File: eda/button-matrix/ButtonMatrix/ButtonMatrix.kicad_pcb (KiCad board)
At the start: 2 copper layers, 87.2 x 87.2 mm, 53 parts, among them SW1 SW_Omron_B3FS, SW10 SW_Omron_B3FS, SW11 SW_Omron_B3FS, SW12 SW_Omron_B3FS, SW13 SW_Omron_B3FS, SW14 SW_Omron_B3FS, SW15 SW_Omron_B3FS, SW16 SW_Omron_B3FS, SW2 SW_Omron_B3FS, SW3 SW_Omron_B3FS, SW4 SW_Omron_B3FS, SW5 SW_Omron_B3FS, SW6 SW_Omron_B3FS, SW7 SW_Omron_B3FS, SW8 SW_Omron_B3FS, SW9 SW_Omron_B3FS

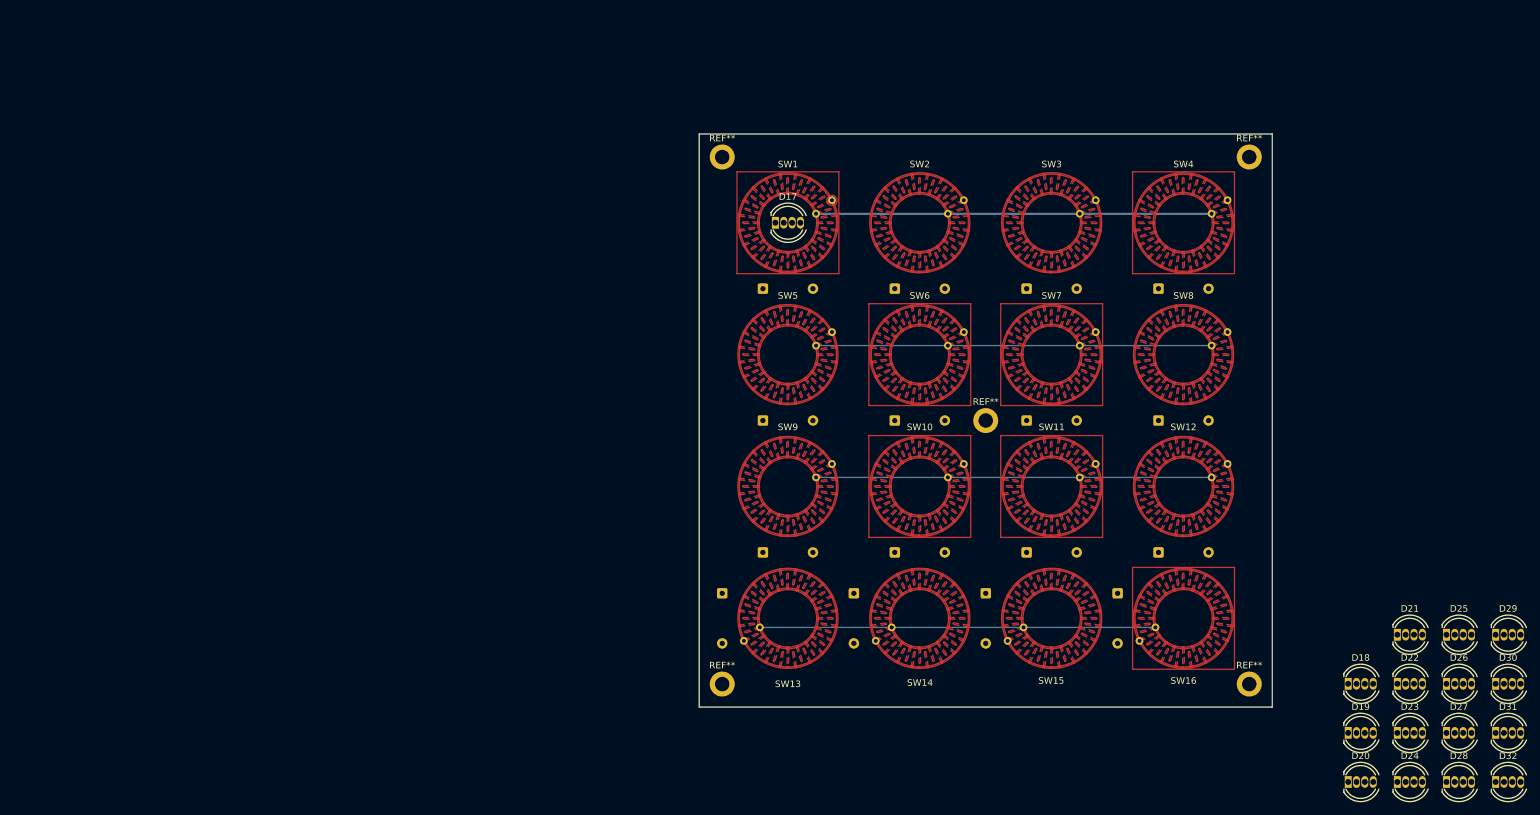
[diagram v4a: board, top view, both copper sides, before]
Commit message: - Added headers and connected all diods
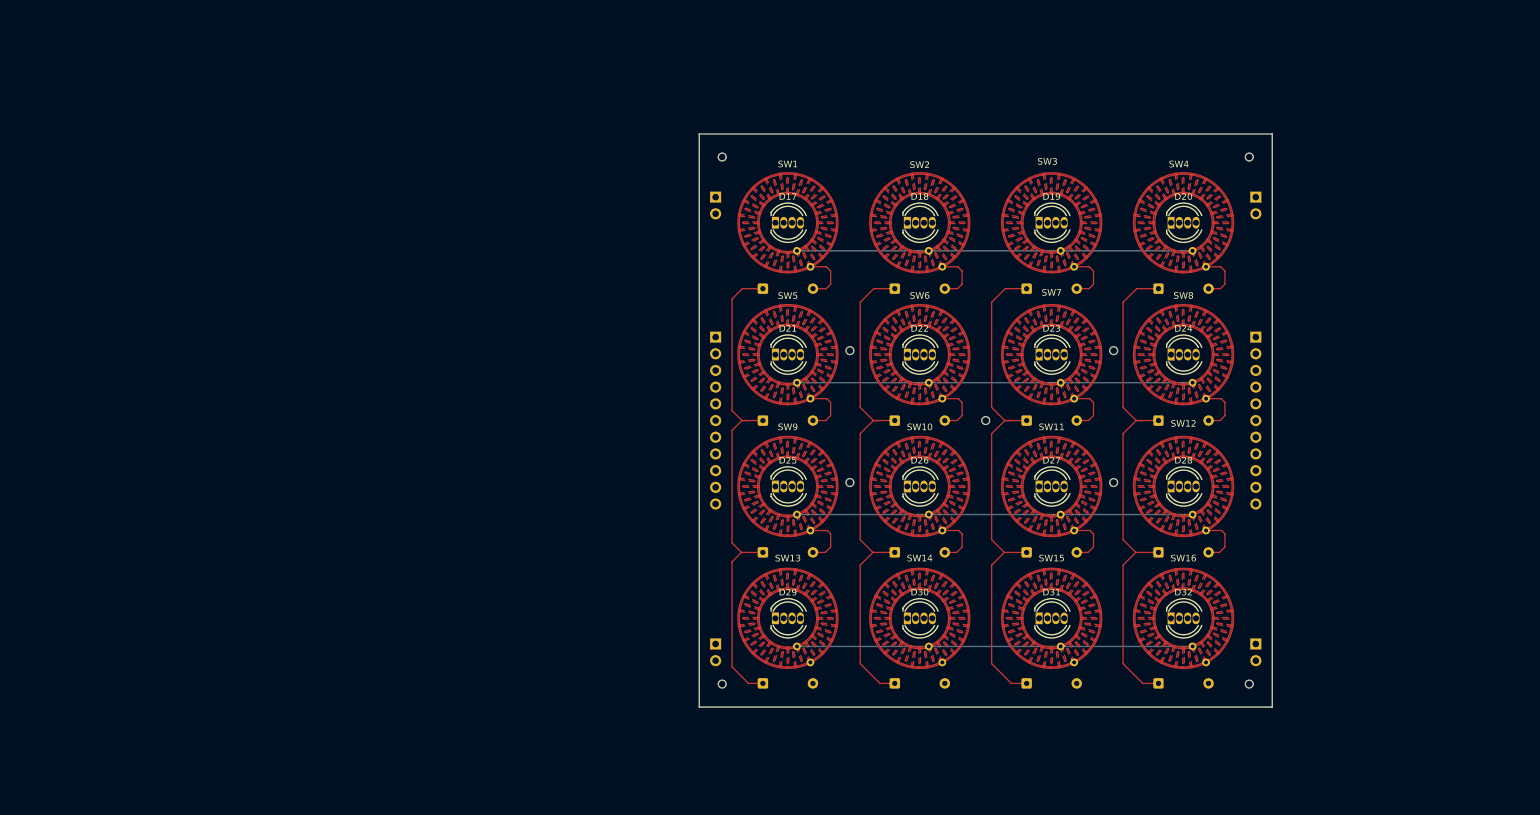
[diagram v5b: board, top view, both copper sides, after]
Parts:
- removed the REF** at (131.5, 62.9)
- removed the REF** at (211.7, 143.1)
- removed the REF** at (131.5, 143.1)
- removed the REF** at (171.6, 103.0)
- removed the REF** at (211.7, 62.9)
- added J1: Conn_01x12, Connector_PinHeader_2.54mm:PinHeader_1x11_P2.54mm_Vertical, B.Cu at (212.7, 90.3)
- added J2: Conn_01x12, Connector_PinHeader_2.54mm:PinHeader_1x11_P2.54mm_Vertical, B.Cu at (130.5, 90.3)
- added REF**: PinHeader_1x02_P2.54mm_Vertical, Connector_PinHeader_2.54mm:PinHeader_1x02_P2.54mm_Vertical, B.Cu at (130.5, 137.0)
- added REF**: PinHeader_1x02_P2.54mm_Vertical, Connector_PinHeader_2.54mm:PinHeader_1x02_P2.54mm_Vertical, B.Cu at (212.7, 69.0)
- added REF**: PinHeader_1x02_P2.54mm_Vertical, Connector_PinHeader_2.54mm:PinHeader_1x02_P2.54mm_Vertical, B.Cu at (212.7, 137.0)
- added REF**: PinHeader_1x02_P2.54mm_Vertical, Connector_PinHeader_2.54mm:PinHeader_1x02_P2.54mm_Vertical, B.Cu at (130.5, 69.0)
- moved D29 109.6 mm to (139.6, 133.1)
- moved D25 104.6 mm to (139.6, 113.0)
- moved D21 103.8 mm to (139.6, 93.0)
- moved D18 97.1 mm to (159.7, 72.9)
- moved D19 90.8 mm to (179.7, 72.9)
- moved D30 90.1 mm to (159.7, 133.1)
- moved D22 89.8 mm to (159.7, 93.0)
- moved D20 89.3 mm to (199.8, 72.9)
- moved D26 87.4 mm to (159.7, 113.0)
- moved D23 79.3 mm to (179.7, 93.0)
- moved D24 73.6 mm to (199.8, 93.0)
- moved D27 72.4 mm to (179.7, 113.0)
- moved D31 71.6 mm to (179.7, 133.1)
- moved D28 61.5 mm to (199.8, 113.0)
- moved D32 55.3 mm to (199.8, 133.1)
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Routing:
- net /SW_COL4: track 0.00 -> 79.0 mm
- net /SW_COL3: track 0.00 -> 78.7 mm
- net /SW_COL2: track 0.00 -> 78.5 mm
- net /SW_COL1: track 0.00 -> 76.9 mm
- net Net-(D9-A): track 0.00 -> 8.32 mm
- net Net-(D1-A): track 0.00 -> 8.32 mm
- net Net-(D5-A): track 0.00 -> 8.32 mm
- net Net-(D10-A): track 0.00 -> 8.18 mm
- net Net-(D2-A): track 0.00 -> 8.18 mm
- net Net-(D6-A): track 0.00 -> 8.18 mm
- net Net-(D11-A): track 0.00 -> 8.05 mm
- net Net-(D3-A): track 0.00 -> 8.05 mm
- net Net-(D7-A): track 0.00 -> 8.05 mm
- net Net-(D12-A): track 0.00 -> 7.92 mm
- net Net-(D4-A): track 0.00 -> 7.92 mm
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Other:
- outline, holes or cut-outs redrawn

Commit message: - Updated PCB more
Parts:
- J1, J2: footprint Connector_PinHeader_2.54mm:PinHeader_1x11_P2.54mm_Vertical -> Connector_PinHeader_2.54mm:PinHeader_1x12_P2.54mm_Vertical
- moved D17 2.69 mm to (141.5, 74.8), turned to 90 degrees
- moved D18 2.69 mm to (161.6, 74.8), turned to 90 degrees
- moved D19 2.69 mm to (181.6, 74.8), turned to 90 degrees
- moved D20 2.69 mm to (201.7, 74.8), turned to 90 degrees
- moved D21 2.69 mm to (141.5, 94.9), turned to 90 degrees
- moved D22 2.69 mm to (161.6, 94.9), turned to 90 degrees
- moved D23 2.69 mm to (181.6, 94.9), turned to 90 degrees
- moved D24 2.69 mm to (201.7, 94.9), turned to 90 degrees
- moved D25 2.69 mm to (141.5, 114.9), turned to 90 degrees
- moved D26 2.69 mm to (161.6, 114.9), turned to 90 degrees
- moved D27 2.69 mm to (181.6, 114.9), turned to 90 degrees
- moved D28 2.69 mm to (201.7, 114.9), turned to 90 degrees
- moved D29 2.69 mm to (141.5, 135.0), turned to 90 degrees
- moved D30 2.69 mm to (161.6, 135.0), turned to 90 degrees
- moved D31 2.69 mm to (181.6, 135.0), turned to 90 degrees
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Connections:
- D17 pad 1: unconnected-(D17-BK-Pad1) -> /LED_B1
- D17 pad 2: unconnected-(D17-GK-Pad2) -> /LED_G1
- D17 pad 3: unconnected-(D17-A-Pad3) -> /LED_COL1
- D17 pad 4: unconnected-(D17-RK-Pad4) -> /LED_R1
- D18 pad 1: unconnected-(D18-BK-Pad1) -> /LED_B1
- D18 pad 2: unconnected-(D18-GK-Pad2) -> /LED_G1
- D18 pad 3: unconnected-(D18-A-Pad3) -> /LED_COL2
- D18 pad 4: unconnected-(D18-RK-Pad4) -> /LED_R1
- D19 pad 1: unconnected-(D19-BK-Pad1) -> /LED_B1
- D19 pad 2: unconnected-(D19-GK-Pad2) -> /LED_G1
- D19 pad 3: unconnected-(D19-A-Pad3) -> /LED_COL3
- D19 pad 4: unconnected-(D19-RK-Pad4) -> /LED_R1
- D20 pad 1: unconnected-(D20-BK-Pad1) -> /LED_B1
- D20 pad 2: unconnected-(D20-GK-Pad2) -> /LED_G1
- D20 pad 3: unconnected-(D20-A-Pad3) -> /LED_COL4
- D20 pad 4: unconnected-(D20-RK-Pad4) -> /LED_R1
- D21 pad 1: unconnected-(D21-BK-Pad1) -> /LED_B2
- D21 pad 2: unconnected-(D21-GK-Pad2) -> /LED_G2
- D21 pad 3: unconnected-(D21-A-Pad3) -> /LED_COL1
- D21 pad 4: unconnected-(D21-RK-Pad4) -> /LED_R2
- D22 pad 1: unconnected-(D22-BK-Pad1) -> /LED_B2
- D22 pad 2: unconnected-(D22-GK-Pad2) -> /LED_G2
- D22 pad 3: unconnected-(D22-A-Pad3) -> /LED_COL2
- D22 pad 4: unconnected-(D22-RK-Pad4) -> /LED_R2
- D23 pad 1: unconnected-(D23-BK-Pad1) -> /LED_B2
- D23 pad 2: unconnected-(D23-GK-Pad2) -> /LED_G2
- D23 pad 3: unconnected-(D23-A-Pad3) -> /LED_COL3
- D23 pad 4: unconnected-(D23-RK-Pad4) -> /LED_R2
- D24 pad 1: unconnected-(D24-BK-Pad1) -> /LED_B2
- D24 pad 2: unconnected-(D24-GK-Pad2) -> /LED_G2
- D24 pad 3: unconnected-(D24-A-Pad3) -> /LED_COL4
- D24 pad 4: unconnected-(D24-RK-Pad4) -> /LED_R2
- D25 pad 1: unconnected-(D25-BK-Pad1) -> /LED_B3
- D25 pad 2: unconnected-(D25-GK-Pad2) -> /LED_G3
- D25 pad 3: unconnected-(D25-A-Pad3) -> /LED_COL1
- D25 pad 4: unconnected-(D25-RK-Pad4) -> /LED_R3
- D26 pad 1: unconnected-(D26-BK-Pad1) -> /LED_B3
- D26 pad 2: unconnected-(D26-GK-Pad2) -> /LED_G3
- D26 pad 3: unconnected-(D26-A-Pad3) -> /LED_COL2
- D26 pad 4: unconnected-(D26-RK-Pad4) -> /LED_R3
- D27 pad 1: unconnected-(D27-BK-Pad1) -> /LED_B3
- D27 pad 2: unconnected-(D27-GK-Pad2) -> /LED_G3
- D27 pad 3: unconnected-(D27-A-Pad3) -> /LED_COL3
- D27 pad 4: unconnected-(D27-RK-Pad4) -> /LED_R3
- D28 pad 1: unconnected-(D28-BK-Pad1) -> /LED_B3
- D28 pad 2: unconnected-(D28-GK-Pad2) -> /LED_G3
- D28 pad 3: unconnected-(D28-A-Pad3) -> /LED_COL4
- D28 pad 4: unconnected-(D28-RK-Pad4) -> /LED_R3
- D29 pad 1: unconnected-(D29-BK-Pad1) -> /LED_B4
- D29 pad 2: unconnected-(D29-GK-Pad2) -> /LED_G4
- D29 pad 3: unconnected-(D29-A-Pad3) -> /LED_COL1
- D29 pad 4: unconnected-(D29-RK-Pad4) -> /LED_R4
- D30 pad 1: unconnected-(D30-BK-Pad1) -> /LED_B4
- D30 pad 2: unconnected-(D30-GK-Pad2) -> /LED_G4
- D30 pad 3: unconnected-(D30-A-Pad3) -> /LED_COL2
- D30 pad 4: unconnected-(D30-RK-Pad4) -> /LED_R4
- D31 pad 1: unconnected-(D31-BK-Pad1) -> /LED_B4
- D31 pad 2: unconnected-(D31-GK-Pad2) -> /LED_G4
- D31 pad 3: unconnected-(D31-A-Pad3) -> /LED_COL3
- D31 pad 4: unconnected-(D31-RK-Pad4) -> /LED_R4
- D32 pad 1: unconnected-(D32-BK-Pad1) -> /LED_B4
- D32 pad 2: unconnected-(D32-GK-Pad2) -> /LED_G4
- D32 pad 3: unconnected-(D32-A-Pad3) -> /LED_COL4
- D32 pad 4: unconnected-(D32-RK-Pad4) -> /LED_R4
- J1 pad 1: unconnected-(J1-Pin_1-Pad1) -> /SW_ROW1
- J1 pad 10: unconnected-(J1-Pin_10-Pad10) -> /LED_COL2
- J1 pad 11: unconnected-(J1-Pin_11-Pad11) -> /LED_COL3
- J1 pad 2: unconnected-(J1-Pin_2-Pad2) -> /SW_ROW2
- J1 pad 3: unconnected-(J1-Pin_3-Pad3) -> /SW_ROW3
- J1 pad 4: unconnected-(J1-Pin_4-Pad4) -> /SW_ROW4
- J1 pad 5: unconnected-(J1-Pin_5-Pad5) -> /SW_COL1
- J1 pad 6: unconnected-(J1-Pin_6-Pad6) -> /SW_COL2
- J1 pad 7: unconnected-(J1-Pin_7-Pad7) -> /SW_COL3
- J1 pad 8: unconnected-(J1-Pin_8-Pad8) -> /SW_COL4
- J1 pad 9: unconnected-(J1-Pin_9-Pad9) -> /LED_COL1
- J2 pad 1: unconnected-(J2-Pin_1-Pad1) -> /LED_R1
- J2 pad 10: unconnected-(J2-Pin_10-Pad10) -> /LED_R4
- J2 pad 11: unconnected-(J2-Pin_11-Pad11) -> /LED_G4
- J2 pad 2: unconnected-(J2-Pin_2-Pad2) -> /LED_G1
- J2 pad 3: unconnected-(J2-Pin_3-Pad3) -> /LED_B1
- J2 pad 4: unconnected-(J2-Pin_4-Pad4) -> /LED_R2
- J2 pad 5: unconnected-(J2-Pin_5-Pad5) -> /LED_G2
- J2 pad 6: unconnected-(J2-Pin_6-Pad6) -> /LED_B2
- J2 pad 7: unconnected-(J2-Pin_7-Pad7) -> /LED_R3
- J2 pad 8: unconnected-(J2-Pin_8-Pad8) -> /LED_G3
- J2 pad 9: unconnected-(J2-Pin_9-Pad9) -> /LED_B3
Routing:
- net /LED_COL2: track 0.00 -> 102.4 mm, vias 0 -> 4
- net /LED_COL1: track 0.00 -> 101.7 mm, vias 0 -> 4
- net /LED_COL4: track 0.00 -> 99.8 mm, vias 0 -> 4
- net /LED_COL3: track 0.00 -> 98.3 mm, vias 0 -> 4
- net /LED_B1: track 0.00 -> 87.2 mm
- net /LED_B4: track 0.00 -> 86.9 mm
- net /LED_R4: track 0.00 -> 86.5 mm
- net /LED_G1: track 0.00 -> 86.0 mm
- net /LED_G4: track 0.00 -> 85.6 mm
- net /LED_R1: track 0.00 -> 84.9 mm
- net /LED_B2: track 0.00 -> 74.0 mm
- net /LED_R3: track 0.00 -> 74.0 mm
- net /LED_G3: track 0.00 -> 74.0 mm
- net /LED_R2: track 0.00 -> 73.5 mm
- net /LED_G2: track 0.00 -> 73.5 mm
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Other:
- outline, holes or cut-outs redrawn

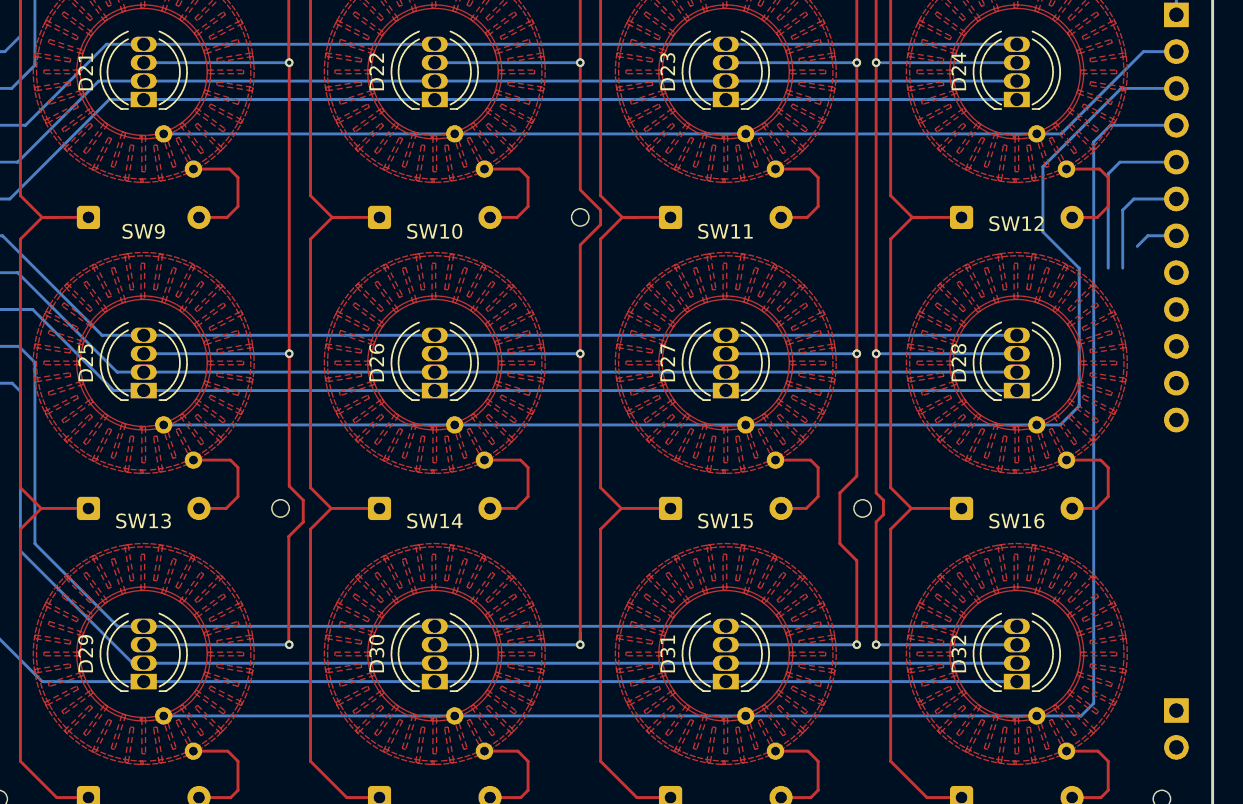
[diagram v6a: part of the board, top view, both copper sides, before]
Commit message: - Connected led grounds
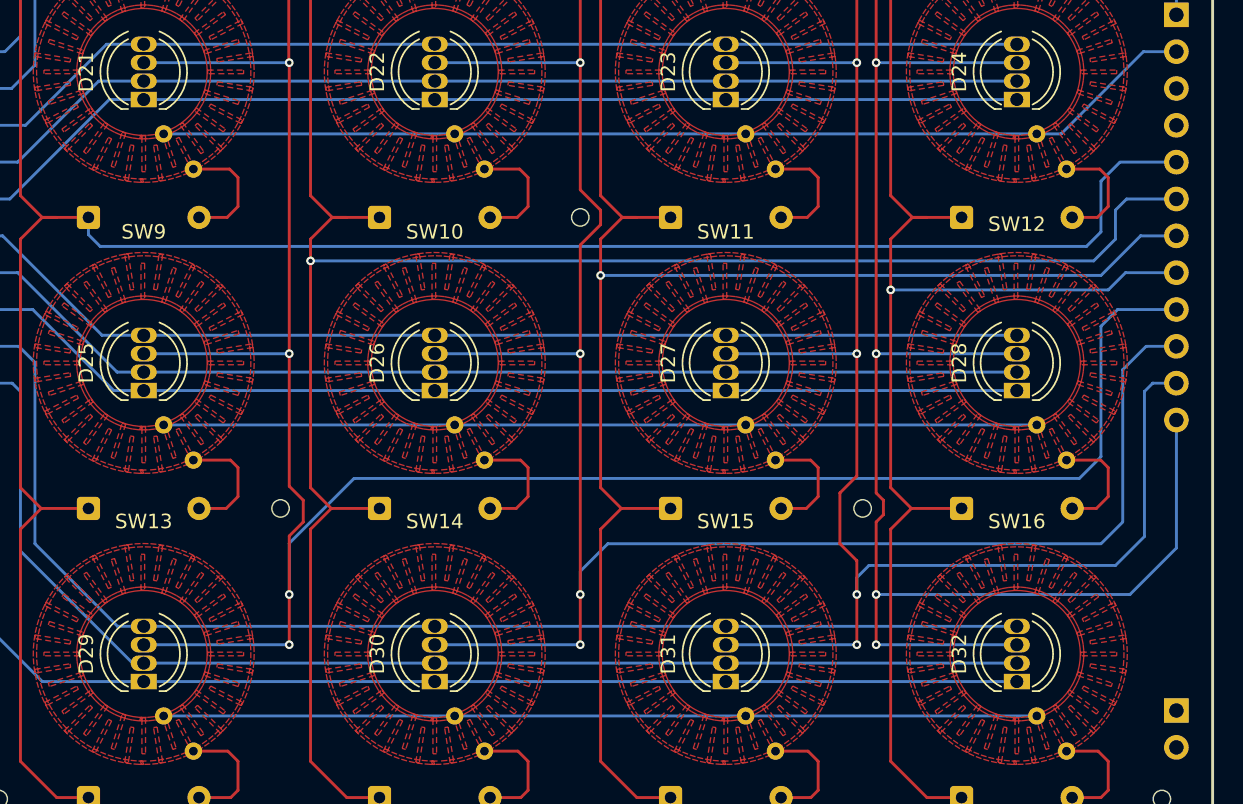
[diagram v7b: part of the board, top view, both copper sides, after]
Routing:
- net /LED_COL1: track 101.7 -> 178.4 mm, vias 4 -> 5
- net /SW_COL1: track 88.5 -> 157.9 mm
- net /SW_COL2: track 85.2 -> 139.8 mm, vias 0 -> 1
- net /LED_COL2: track 102.4 -> 156.8 mm, vias 4 -> 5
- net /SW_ROW4: track 109.4 -> 60.2 mm
- net /SW_COL3: track 80.5 -> 118.3 mm, vias 0 -> 1
- net /LED_COL3: track 98.3 -> 132.9 mm, vias 4 -> 5
- net /SW_ROW3: track 92.6 -> 60.2 mm
- net /LED_COL4: track 99.8 -> 130.7 mm, vias 4 -> 5
- net /SW_COL4: track 77.7 -> 97.9 mm, vias 0 -> 1
